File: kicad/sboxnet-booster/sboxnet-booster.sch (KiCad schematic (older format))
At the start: 52 parts, among them J1 sboxnet-stecker_02x17, J3 Conn_01x02_Male, J4 Conn_01x02_Male, J5 Screw_Terminal_01x04, J6 Screw_Terminal_01x04, J7 Power von externen 15V/4A Net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, SW1 Öffner, U1 L6206PSO-sboxnet, U2 L78L12_SOT89

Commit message: sboxnet booster finished
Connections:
- net PD0: now also R1.2; no longer R3.2
- net PD2: now also R3.2; no longer R1.2
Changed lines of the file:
@@
 	1    0    0    -1
 $EndComp
-Text GLabel 1890 1870 3    39   Input ~ 0
+Text GLabel 800  1850 3    39   Input ~ 0
 PD0
 $Comp
@@
 	1    0    0    -1
 $EndComp
-Text GLabel 800  1850 3    39   Input ~ 0
+Text GLabel 1890 1870 3    39   Input ~ 0
 PD2
 Wire Wire Line

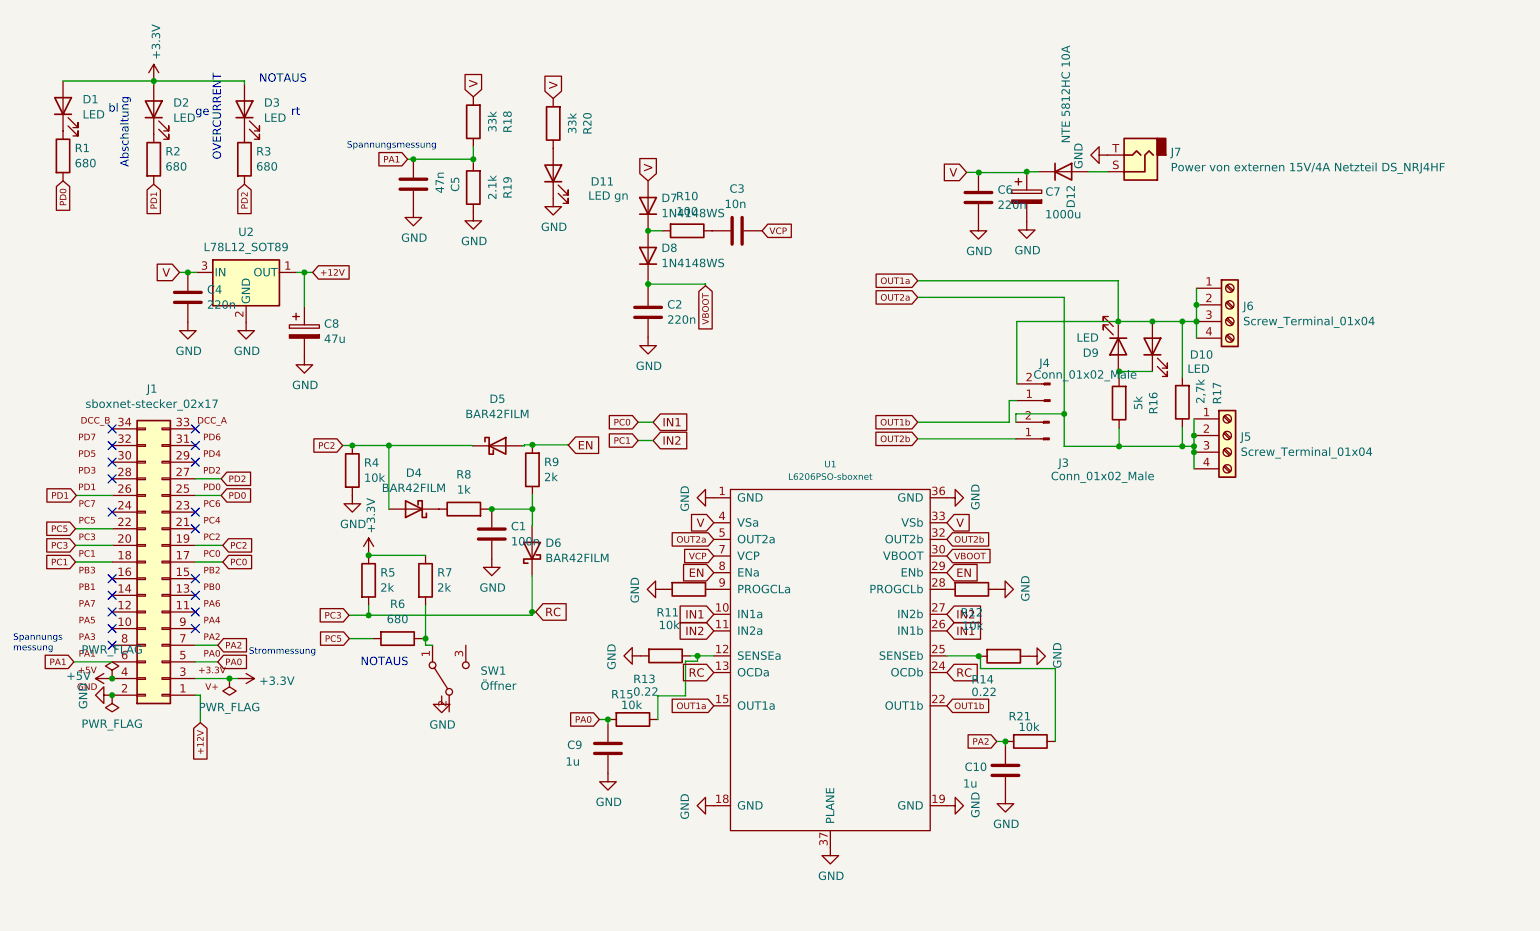
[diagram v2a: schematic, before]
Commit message: booster DCC Input
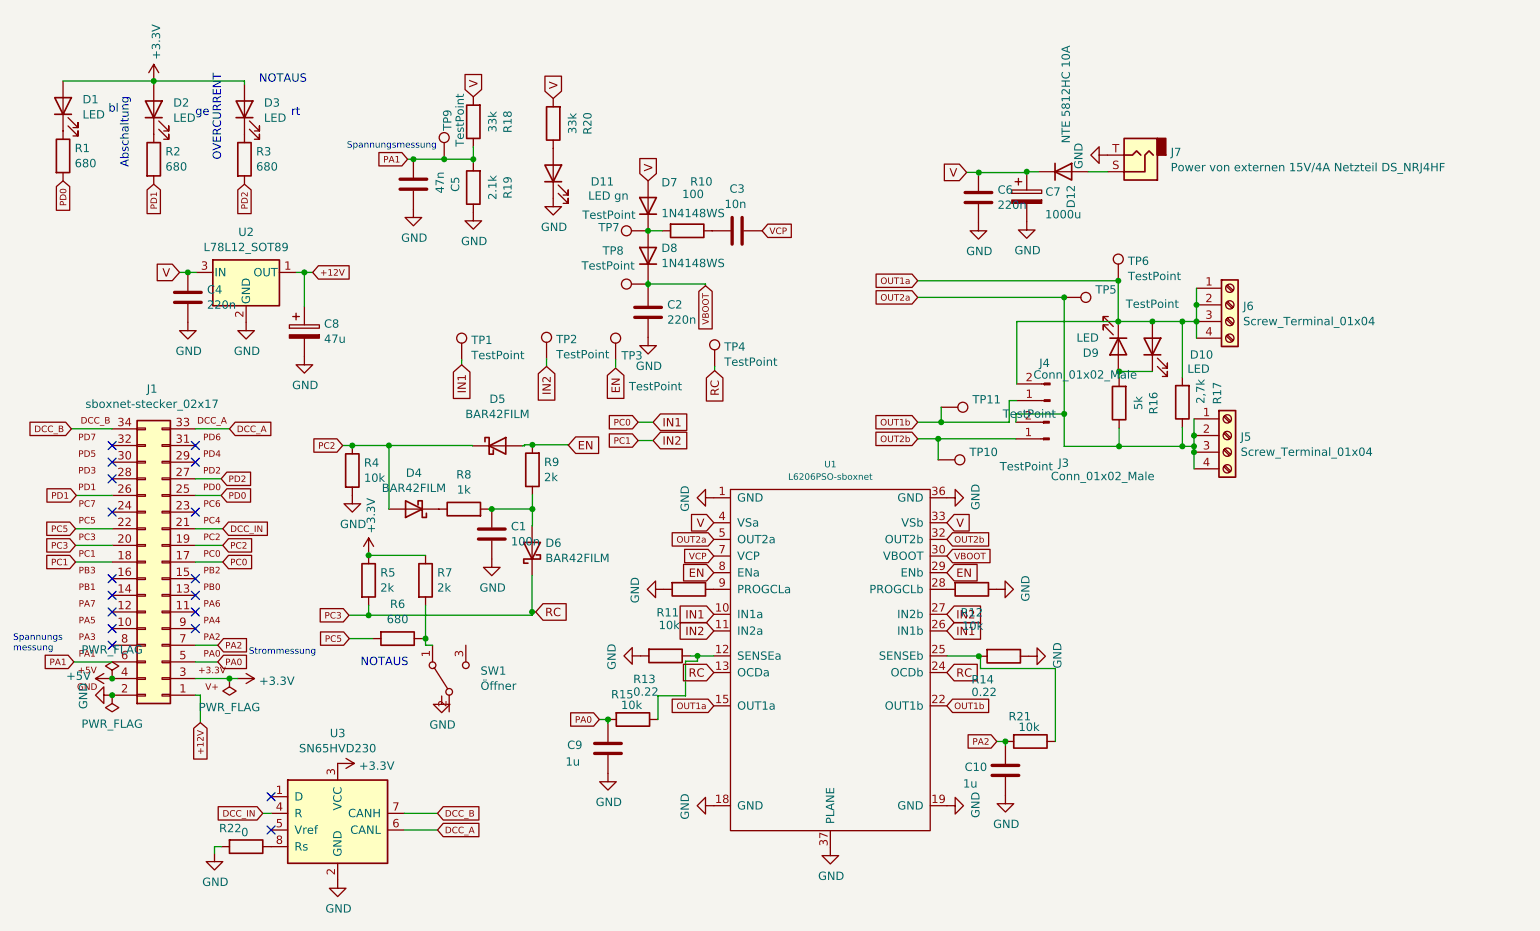
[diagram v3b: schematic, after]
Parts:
- added R22: 0, Resistor_SMD:R_1206_3216Metric, symbol Device:R
- added TP1, TP10, TP11, TP2, TP3, TP4, TP5, TP6, TP7, TP8, TP9: TestPoint, Connector_PinHeader_2.54mm:PinHeader_1x01_P2.54mm_Vertical, symbol Connector:TestPoint
- added U3: SN65HVD230, Package_SO:SOIC-8_3.9x4.9mm_P1.27mm, symbol Interface_CAN_LIN:SN65HVD230
- U1: footprint Package_SO:HSOP-36-1EP_11.0x15.9mm_P0.65mm_SlugDown_ThermalVias -> sboxnet:HSOP-36-1EP_11.0x15.9mm_P0.65mm_SlugDown_ThermalVias
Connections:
- net +3V3: now also U3.3 (VCC)
- net EN: now also TP3.1
- net GND: now also R22.2, U3.2 (GND)
- net IN1: now also TP1.1
- net IN2: now also TP2.1
- net OUT1a: now also TP6.1
- net OUT1b: now also TP11.1
- net OUT2a: now also TP5.1
- net OUT2b: now also TP10.1
- net PA1: now also TP9.1
- net PC3: now also TP4.1
- net VBOOT: now also TP8.1
- net at D7.1 (K), D8.2 (A), R10.2: now also TP7.1
- net DCC_IN: now reaches J1.21 (Pin_21)
- net DCC_IN: now also U3.4 (R)
- net DCC_A: now reaches J1.33 (Pin_33)
- net DCC_A: now also U3.6 (CANL)
- net DCC_B: now reaches J1.34 (Pin_34)
- net DCC_B: now also U3.7 (CANH)
- new net: R22.1, U3.8 (Rs)
- no-connect marks 19 -> 18

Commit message: booster cleanup, sboxnet-booster add on led
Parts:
- added D13: LED, LED_THT:LED_D3.0mm, symbol Device:LED
- added R23: 680, Resistor_SMD:R_1206_3216Metric, symbol Device:R
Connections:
- net +3V3: now also D13.2 (A)
- net GND: now also SW1.2 (B)
- net PD3: now reaches J1.28 (Pin_28)
- net PD3: now also R23.2
- net DCC_IN: no longer names the net of J1.21 (Pin_21), U3.4 (R)
- new net: D13.1 (K), R23.1
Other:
- moved on the sheet: C4, C6, C8, J1, U2
